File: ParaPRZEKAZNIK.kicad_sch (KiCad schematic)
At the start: 50 parts, among them J101 Screw_Terminal_01x03, J102 Screw_Terminal_01x03, J103 Screw_Terminal_01x03, J104 Screw_Terminal_01x03, J105 Screw_Terminal_01x03, J106 RJ45, U101 MAX31865xTP, U102 ST3232BTR, Y101 32k768

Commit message: schematic
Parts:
- added C1, C10, C15, C16, C2, C4, C6, C8, C9: 100n, Capacitor_SMD:C_0805_2012Metric_Pad1.18x1.45mm_HandSolder, symbol Device:C_Small
- added C13, C17: 1uF, Capacitor_SMD:C_0805_2012Metric_Pad1.18x1.45mm_HandSolder, symbol Device:C_Small
- added C14: 22uF, Capacitor_THT:CP_Radial_D8.0mm_P5.00mm, symbol Device:C_Polarized
- added C18: 100uF, Capacitor_THT:CP_Radial_D8.0mm_P5.00mm, symbol Device:C_Polarized
- added D1: 1N4001, Diode_THT:D_DO-41_SOD81_P10.16mm_Horizontal, symbol Diode:1N4001
- added D2: 1.0SMBJ5.0A, Diode_SMD:D_SMB, symbol Diode:SM6T6V8A
- added J1: PT1000, Connector_Phoenix_MC:PhoenixContact_MCV_1,5_4-G-3.81_1x04_P3.81mm_Vertical, symbol Connector:Screw_Terminal_01x04
- added J3: UC_CONTROL, Connector_Phoenix_MC:PhoenixContact_MCV_1,5_2-G-3.5_1x02_P3.50mm_Vertical, symbol Connector:Screw_Terminal_01x02
- added J4: MAIN_CONTROL, Connector_Phoenix_MC:PhoenixContact_MCV_1,5_3-G-3.5_1x03_P3.50mm_Vertical, symbol Connector:Screw_Terminal_01x03
- added J5: PROG, Connector_PinHeader_2.54mm:PinHeader_1x06_P2.54mm_Vertical, symbol Connector_Generic:Conn_01x06
- added L1, L2, L3, L4, L5: 4u7, Inductor_SMD:L_0805_2012Metric_Pad1.15x1.40mm_HandSolder, symbol Device:L_Ferrite
- added R1: 630, Resistor_SMD:R_0805_2012Metric_Pad1.20x1.40mm_HandSolder, symbol Device:R
- added R10, R11, R3, R5, R6: 10k, Resistor_SMD:R_0805_2012Metric_Pad1.20x1.40mm_HandSolder, symbol Device:R
- added R12, R13: 10k, Resistor_SMD:R_0805_2012Metric_Pad1.20x1.40mm_HandSolder, symbol Device:R_Small
- added R2: 120, Resistor_SMD:R_0805_2012Metric_Pad1.20x1.40mm_HandSolder, symbol Device:R
- added U2: SP3485EN, Package_SO:SOIC-8_3.9x4.9mm_P1.27mm, symbol Interface_UART:SP3485EN
- added U5: LM1117DT-3.3, Package_TO_SOT_SMD:TO-252-3_TabPin2, symbol Regulator_Linear:LM1117DT-3.3
- C11: renamed from C?; footprint (none) -> Capacitor_SMD:C_0805_2012Metric_Pad1.18x1.45mm_HandSolder
- C12: renamed from C103; value C -> 100n; footprint (none) -> Capacitor_SMD:C_0805_2012Metric_Pad1.18x1.45mm_HandSolder
- C19: renamed from C101; footprint (none) -> Capacitor_SMD:C_0805_2012Metric_Pad1.18x1.45mm_HandSolder
- C20: renamed from C102; footprint (none) -> Capacitor_SMD:C_0805_2012Metric_Pad1.18x1.45mm_HandSolder
- C3: renamed from C106; value C -> 100n; footprint (none) -> Capacitor_SMD:C_0805_2012Metric_Pad1.18x1.45mm_HandSolder
- C5: renamed from C105; value C -> 100n; footprint (none) -> Capacitor_SMD:C_0805_2012Metric_Pad1.18x1.45mm_HandSolder
- C7: renamed from C104; value C -> 100n; footprint (none) -> Capacitor_SMD:C_0805_2012Metric_Pad1.18x1.45mm_HandSolder
- D10, D11, D12, D13, D14: renamed from D?; value D_Schottky -> 1N5819HW-7-F; footprint (none) -> Diode_SMD:D_SOD-123
- J10: renamed from J105; footprint (none) -> Connector_Phoenix_MSTB:PhoenixContact_MSTBVA_2,5_3-G_1x03_P5.00mm_Vertical
- J2: renamed from J106; value RJ45 -> 5556416-1 TE Connectivity; footprint (none) -> Connector_RJ:RJ45_OST_PJ012-8P8CX_Vertical
- J6: renamed from J101; footprint (none) -> Connector_Phoenix_MSTB:PhoenixContact_MSTBVA_2,5_3-G_1x03_P5.00mm_Vertical
- J7: renamed from J102; footprint (none) -> Connector_Phoenix_MSTB:PhoenixContact_MSTBVA_2,5_3-G_1x03_P5.00mm_Vertical
- J8: renamed from J103; footprint (none) -> Connector_Phoenix_MSTB:PhoenixContact_MSTBVA_2,5_3-G_1x03_P5.00mm_Vertical
- J9: renamed from J104; footprint (none) -> Connector_Phoenix_MSTB:PhoenixContact_MSTBVA_2,5_3-G_1x03_P5.00mm_Vertical
- R4, R7, R8, R9: renamed from R?; footprint (none) -> Resistor_SMD:R_0805_2012Metric_Pad1.20x1.40mm_HandSolder
- RN1, RN2: renamed from RN?; footprint (none) -> Resistor_SMD:R_Array_Convex_4x1206; symbol Device:R_Pack05 -> Device:R_Pack04
- SW1: renamed from SW?; footprint (none) -> switches:Alps_SSSS222700
- U3: renamed from U102; footprint (none) -> Package_SO:TSSOP-16_4.4x5mm_P0.65mm
- U6: renamed from U?; footprint (none) -> Package_SO:TSOP-6_1.65x3.05mm_P0.95mm
- Y1: renamed from Y101; footprint (none) -> Crystal:Crystal_SMD_SeikoEpson_MC306-4Pin_8.0x3.2mm
- gave numbers to parts that had none: 19
- renumbered U101 to U1
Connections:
- net +5V is gone; now on net +3V3: R9.2
- net VCC is gone; now on net +3V3: U6.5 (VCC), U6.5 (VCC)
- net GND: now also J2.4, J2.5, U1.10 (GND), U1.15 (DGND), U1.16 (GND), U1.21 (GND), U3.15 (GND), C1.1, C10.1, C13.1, C14.2, C15.1, C16.1, C17.1, C18.2, C2.1, C4.1, C6.1, C8.1, C9.1, D2.2 (A2), J3.2 (Pin_2), J4.3 (Pin_3), J5.6 (Pin_6), R10.2, R11.2, R3.1, R6.1, U2.5 (GND), U5.1 (GND)
- net RESET: now also J5.5 (Pin_5), R11.1
- net SWCLK: now also J5.4 (Pin_4)
- net SWDIO: now also J5.3 (Pin_3)
- net +12V: now reaches D12.1 (K)
- net +12V: now also D10.1 (K), D11.1 (K), D13.1 (K), D14.1 (K), K1.2, K2.2, K3.2, K4.2, K5.2, C13.2, D1.1 (K), L5.1
- net at D12.2 (A): now also K3.9, Q4.3 (C)
- net CONTROL_SIG: now reaches R4.1
- net CONTROL_SIG: now also J4.2 (Pin_2)
- net USART2_TX: now reaches U3.11 (T1IN)
- net USART2_TX: now also U4.8 (PA2)
- net RS232_RX: now reaches U3.13 (R1IN)
- net RS232_RX: now also J2.6
- net RS232_TX: now reaches U3.14 (T1OUT)
- net RS232_TX: now also J2.3
- net +3V3: now reaches U3.16 (VCC)
- net +3V3: now also U1.19 (DVDD), U1.20 (VDD), U4.1 (VDD), U4.17 (VDD), U4.5 (VDDA), C10.2, C15.2, C16.2, C17.2, C18.1, C9.2, J5.1 (Pin_1), R5.2, U2.8 (VCC), U5.2 (VO)
- net USART2_RX: now reaches U3.9 (R2OUT)
- net USART2_RX: now also U4.9 (PA3)
- net at K5.9, Q6.3 (C): now also D14.2 (A)
- net F+: now reaches U1.5 (FORCE+)
- net F+: now also C1.2, L1.2
- net R+: now reaches U1.7 (RTDIN+)
- net R+: now also C2.2, L3.2
- net R-: now reaches U1.8 (RTDIN-)
- net R-: now also C4.2, L2.2
- net F-: now reaches U1.9 (FORCE-)
- net F-: now also C6.2, L4.2
- net BASE_R4: now reaches RN2.1 (R1.1)
- net BASE_R4: now also Q5.1 (B); no longer Q6.1 (B)
- net RELAYS_CTRL: now reaches D5.2 (A), D6.2 (A), D7.2 (A), D8.2 (A), D9.2 (A), U6.6
- net ACTIVE_HI: now reaches SW1.3 (C), U6.4
- net ACTIVE_LO: now reaches Q1.2 (E), R8.1, R9.1, SW1.1 (A), SW1.4 (A)
- net at K1.9, Q2.3 (C): now also D10.2 (A)
- net at D13.2 (A): now also K4.9, Q5.3 (C)
- net BASE_R1: now reaches RN2.4 (R4.1)
- net BASE_R1: now also Q2.1 (B); no longer Q3.1 (B)
- net at K2.9, Q3.3 (C): now also D11.2 (A)
- net BASE_R3: now reaches RN2.2 (R2.1)
- net BASE_R3: now also Q4.1 (B); no longer Q5.1 (B)
- net UC_R5: now reaches U4.30 (PB7)
- net UC_R5: now also R12.1; no longer RN1.10 (R1.2)
- net UC_R1: now reaches U4.26 (PB3)
- net UC_R1: now also RN1.5 (R4.2); no longer RN1.6 (R5.2)
- net UC_R2: now reaches U4.27 (PB4)
- net UC_R2: now also RN1.6 (R3.2); no longer RN1.7 (R4.2)
- net UC_R3: now reaches U4.28 (PB5)
- net UC_R3: now also RN1.7 (R2.2); no longer RN1.8 (R3.2)
- net UC_R4: now reaches U4.29 (PB6)
- net UC_R4: now also RN1.8 (R1.2); no longer RN1.9 (R2.2)
- net R1: now reaches RN2.5 (R4.2)
- net R1: now also D5.1 (K), RN1.4 (R4.1); no longer Q2.1 (B)
- net MICRO_CTRL: now reaches U4.15 (PB1)
- net MICRO_CTRL: now also C8.2, D2.1 (A1), R1.2, R3.2
- net USART1_TX: now reaches U4.19 (PA9)
- net USART1_TX: now also R6.2, U2.4 (DI)
- net USART1_RX: now reaches U4.20 (PA10)
- net USART1_RX: now also U2.1 (RO)
- net USART1_DE: now reaches U4.22 (PA12)
- net USART1_DE: now also R5.1, U2.2 (~{RE}), U2.3 (DE)
- net BOOT0: now reaches U4.31 (BOOT0)
- net BOOT0: now also J5.2 (Pin_2), R10.1
- net BASE_R2: now reaches RN2.3 (R3.1)
- net BASE_R2: now also Q3.1 (B); no longer Q4.1 (B)
- new net: J3.1 (Pin_1), R1.1
- new net: J1.3 (Pin_3), L2.1
- new net: R2.2, U2.6 (A)
- new net: R2.1, U2.7 (B)
- new net: C14.1, L5.2, U5.3 (VI)
- new net: D1.2 (A), J4.1 (Pin_1)
- new net: J1.1 (Pin_1), L1.1
- new net: J1.2 (Pin_2), L3.1
- new net: J1.4 (Pin_4), L4.1
- new net BASE_R5: Q6.1 (B), R13.2
- new net R2: D6.1 (K), RN1.3 (R3.1), RN2.6 (R3.2)
- new net R3: D7.1 (K), RN1.2 (R2.1), RN2.7 (R2.2)
- new net R4: D8.1 (K), RN1.1 (R1.1), RN2.8 (R1.2)
- new net R5: D9.1 (K), R12.2, R13.1
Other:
- note removed: "ACTIVE HI"
- moved on the sheet: C12, C3, C5, C7, D4, J2, R7, U1, U3, U6B

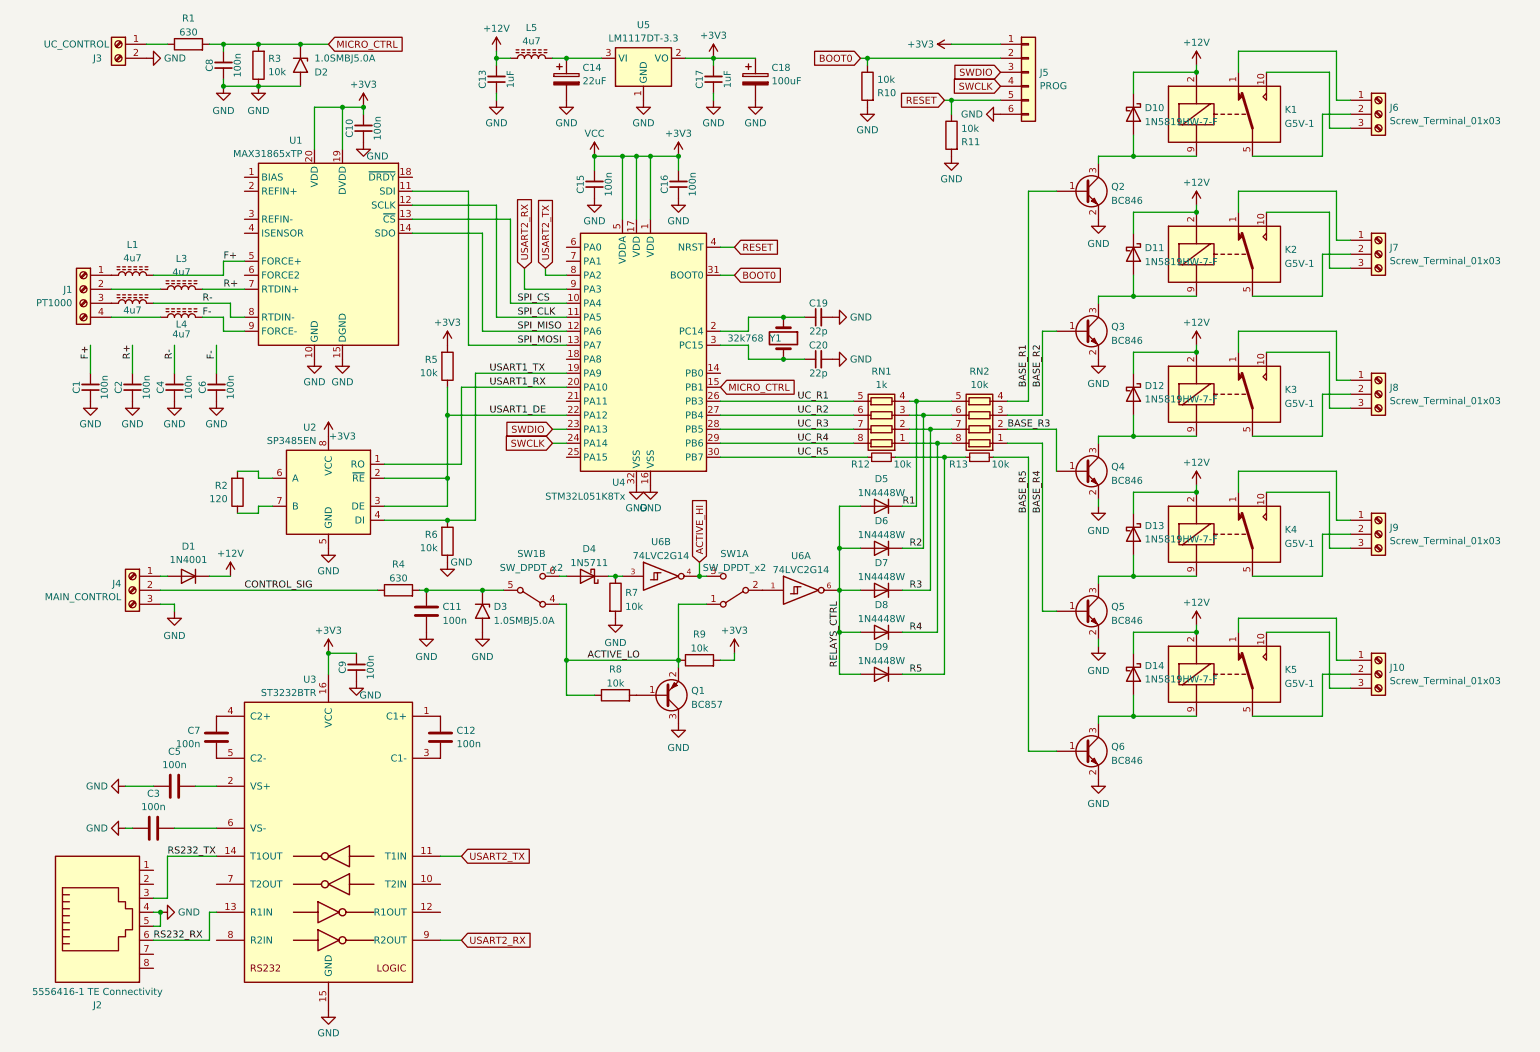
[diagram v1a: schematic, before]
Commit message: componets placed on pcb
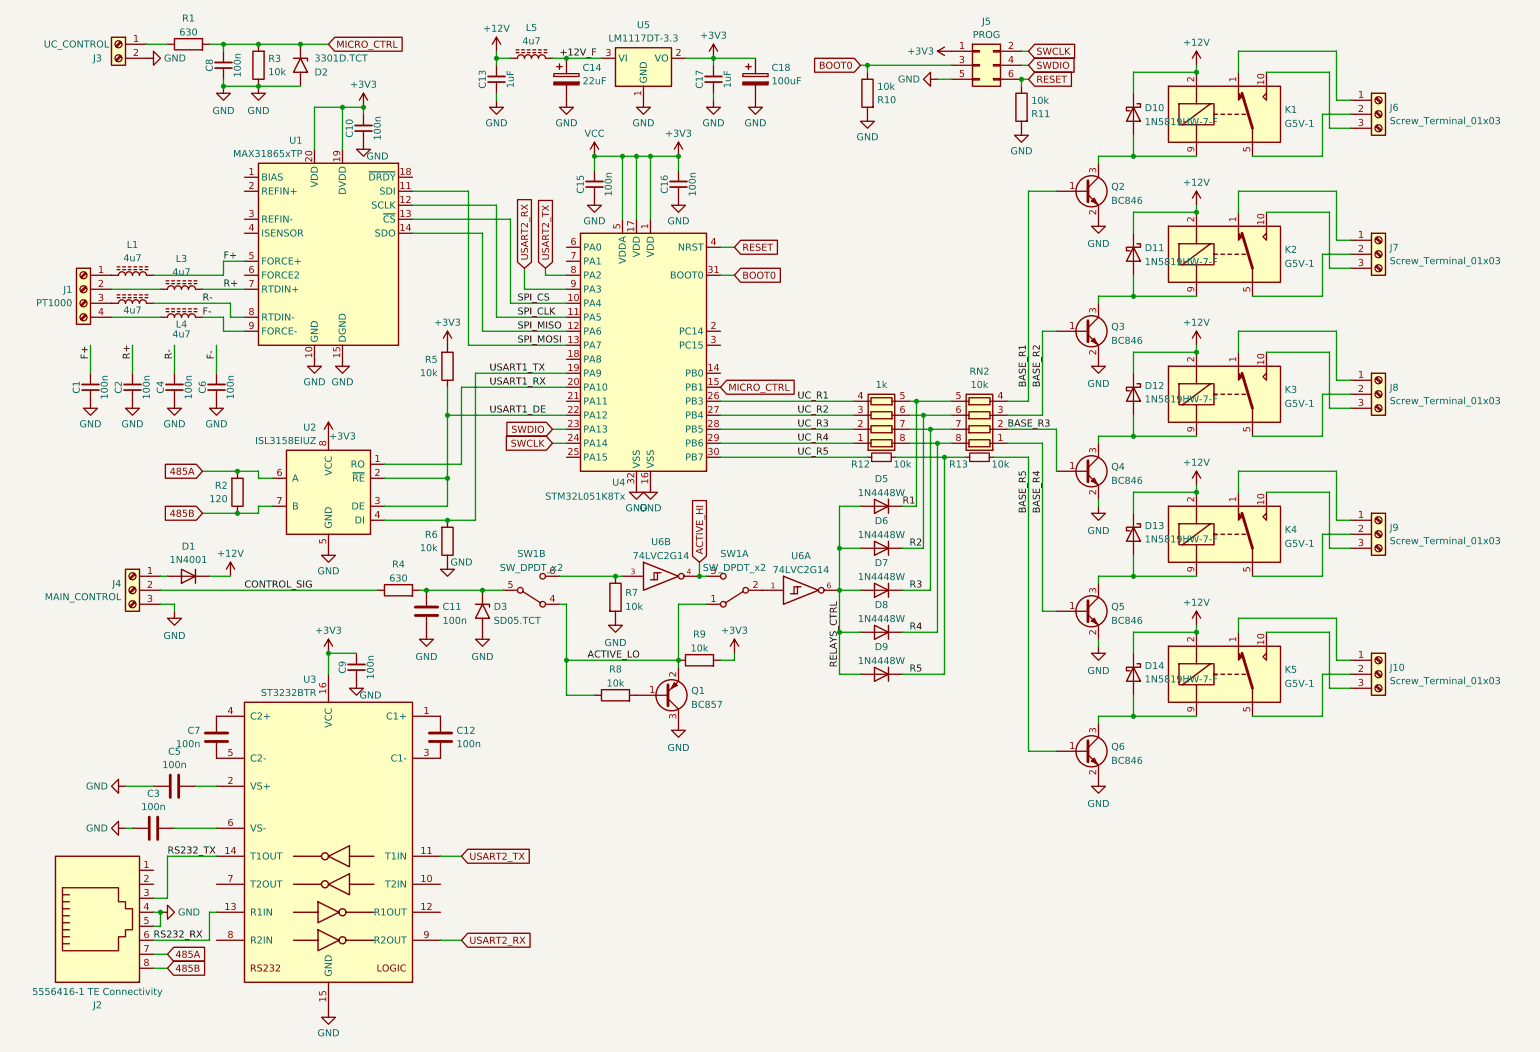
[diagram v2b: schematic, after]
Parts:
- removed C19, C20: 22p, Capacitor_SMD:C_0805_2012Metric_Pad1.18x1.45mm_HandSolder, symbol Device:C_Small
- removed D4: 1N5711, Diode_THT:D_DO-35_SOD27_P7.62mm_Horizontal, symbol Diode:1N5711
- removed Y1: 32k768, Crystal:Crystal_SMD_SeikoEpson_MC306-4Pin_8.0x3.2mm, symbol Device:Crystal
- C18: footprint Capacitor_THT:CP_Radial_D8.0mm_P5.00mm -> Capacitor_Tantalum_SMD:CP_EIA-3528-21_Kemet-B_Pad1.50x2.35mm_HandSolder
- D1: footprint Diode_THT:D_DO-41_SOD81_P10.16mm_Horizontal -> Diode_SMD:D_SMB
- D2: value 1.0SMBJ5.0A -> 3301D.TCT; footprint Diode_SMD:D_SMB -> Diode_SMD:D_SOD-323_HandSoldering
- D3: value 1.0SMBJ5.0A -> SD05.TCT; footprint Diode_SMD:D_SMB -> Diode_SMD:D_SOD-323_HandSoldering
- J10, J6, J7, J8, J9: footprint Connector_Phoenix_MSTB:PhoenixContact_MSTBVA_2,5_3-G_1x03_P5.00mm_Vertical -> Connector_Phoenix_MC:PhoenixContact_MCV_1,5_3-G-3.5_1x03_P3.50mm_Vertical
- J5: footprint Connector_PinHeader_2.54mm:PinHeader_1x06_P2.54mm_Vertical -> Connector_PinHeader_2.54mm:PinHeader_2x03_P2.54mm_Vertical; symbol Connector_Generic:Conn_01x06 -> Connector_Generic:Conn_02x03_Odd_Even
- U2: value SP3485EN -> ISL3158EIUZ; footprint Package_SO:SOIC-8_3.9x4.9mm_P1.27mm -> Package_SO:MSOP-8_3x3mm_P0.65mm
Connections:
- net BOOT0: now also J5.3 (Pin_3); no longer J5.2 (Pin_2)
- net GND: now also J5.5 (Pin_5); no longer J5.6 (Pin_6)
- net R1: now also RN1.5 (R4.2); no longer RN1.4 (R4.1)
- net R2: now also RN1.6 (R3.2); no longer RN1.3 (R3.1)
- net R3: now also RN1.7 (R2.2); no longer RN1.2 (R2.1)
- net R4: now also RN1.8 (R1.2); no longer RN1.1 (R1.1)
- net RESET: now also J5.6 (Pin_6); no longer J5.5 (Pin_5)
- net SWCLK: now also J5.2 (Pin_2); no longer J5.4 (Pin_4)
- net SWDIO: now also J5.4 (Pin_4); no longer J5.3 (Pin_3)
- net UC_R1: now also RN1.4 (R4.1); no longer RN1.5 (R4.2)
- net UC_R2: now also RN1.3 (R3.1); no longer RN1.6 (R3.2)
- net UC_R3: now also RN1.2 (R2.1); no longer RN1.7 (R2.2)
- net UC_R4: now also RN1.1 (R1.1); no longer RN1.8 (R1.2)
- net 485A: now reaches R2.2, U2.6 (A)
- net 485A: now also J2.7
- net 485B: now reaches R2.1, U2.7 (B)
- net 485B: now also J2.8
- net +12V_F: now reaches C14.1, L5.2, U5.3 (VI)
- net at R7.1, U6.3: now also SW1.6 (C)
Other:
- moved on the sheet: J5, R10, R11

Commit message: partially routed
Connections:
- net +12V_F is gone; now on net +12V: C14.1, L5.2, U5.3 (VI)
- net +12V: no longer C13.2, D1.1 (K), L5.1
- net F+: no longer U1.5 (FORCE+)
- new net +BATT: C13.2, D1.1 (K), L5.1
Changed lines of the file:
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@@
+    (stroke (width 0) (type default))
+  )
+  (wire (pts (xy 109.22 19.05) (xy 109.22 20.32))
     (stroke (width 0) (type default))
   )
@@
     (stroke (width 0) (type default))
   )
-  (wire (pts (xy 46.99 57.15) (xy 50.8 57.15))
+  (wire (pts (xy 46.99 57.15) (xy 43.18 57.15))
     (stroke (width 0) (type default))
   )
@@
   )
   (label "BASE_R2" (at 195.58 80.01 90) (fields_autoplaced)
-    (effects (font (size 1.27 1.27)) (justify left bottom))
-  )
-  (label "+12V_F" (at 107.95 20.32 0) (fields_autoplaced)
     (effects (font (size 1.27 1.27)) (justify left bottom))
   )
@@
     )
   )
+  (symbol (lib_id "power:+BATT") (at 48.26 114.3 0) (unit 1)
+    (in_bom yes) (on_board yes) (dnp no) (fields_autoplaced)
+    (property "Reference" "#PWR042" (at 48.26 118.11 0)
+      (effects (font (size 1.27 1.27)) hide)
+    )
+    (property "Value" "+BATT" (at 48.26 110.1669 0)
+      (effects (font (size 1.27 1.27)))
+    )
+    (property "Footprint" "" (at 48.26 114.3 0)
+      (effects (font (size 1.27 1.27)) hide)
+    )
+    (property "Datasheet" "" (at 48.26 114.3 0)
+      (effects (font (size 1.27 1.27)) hide)
+    )
+    (pin "1")
+    (instances
+      (project "ParaPRZEKAZNIK"
+        (path "/e63e39d7-6ac0-4ffd-8aa3-1841a4541b55"
+          (reference "#PWR042") (unit 1)
+        )
+      )
+    )
+  )
   (symbol (lib_id "Device:C_Small") (at 46.99 21.59 180) (unit 1)
     (in_bom yes) (on_board yes) (dnp no)
@@
     )
   )
+  (symbol (lib_id "power:+BATT") (at 96.52 19.05 0) (unit 1)
+    (in_bom yes) (on_board yes) (dnp no) (fields_autoplaced)
+    (property "Reference" "#PWR011" (at 96.52 22.86 0)
+      (effects (font (size 1.27 1.27)) hide)
+    )
+    (property "Value" "+BATT" (at 96.52 14.9169 0)
+      (effects (font (size 1.27 1.27)))
+    )
+    (property "Footprint" "" (at 96.52 19.05 0)
+      (effects (font (size 1.27 1.27)) hide)
+    )
+    (property "Datasheet" "" (at 96.52 19.05 0)
+      (effects (font (size 1.27 1.27)) hide)
+    )
+    (pin "1")
+    (instances
+      (project "ParaPRZEKAZNIK"
+        (path "/e63e39d7-6ac0-4ffd-8aa3-1841a4541b55"
+          (reference "#PWR011") (unit 1)
+        )
+      )
+    )
+  )
   (symbol (lib_id "Device:D_Schottky") (at 212.09 106.68 270) (unit 1)
     (in_bom yes) (on_board yes) (dnp no) (fields_autoplaced)
@@
     )
   )
-  (symbol (lib_id "power:+12V") (at 96.52 19.05 0) (unit 1)
-    (in_bom yes) (on_board yes) (dnp no) (fields_autoplaced)
-    (property "Reference" "#PWR026" (at 96.52 22.86 0)
-      (effects (font (size 1.27 1.27)) hide)
-    )
-    (property "Value" "+12V" (at 96.52 14.9169 0)
-      (effects (font (size 1.27 1.27)))
-    )
-    (property "Footprint" "" (at 96.52 19.05 0)
-      (effects (font (size 1.27 1.27)) hide)
-    )
-    (property "Datasheet" "" (at 96.52 19.05 0)
+  (symbol (lib_id "power:+12V") (at 109.22 19.05 0) (unit 1)
+    (in_bom yes) (on_board yes) (dnp no) (fields_autoplaced)
+    (property "Reference" "#PWR026" (at 109.22 22.86 0)
+      (effects (font (size 1.27 1.27)) hide)
+    )
+    (property "Value" "+12V" (at 109.22 14.9169 0)
+      (effects (font (size 1.27 1.27)))
+    )
+    (property "Footprint" "" (at 109.22 19.05 0)
+      (effects (font (size 1.27 1.27)) hide)
+    )
+    (property "Datasheet" "" (at 109.22 19.05 0)
       (effects (font (size 1.27 1.27)) hide)
     )
@@
         )
       )
-    )
-  )
-  (symbol (lib_id "power:+12V") (at 48.26 114.3 0) (unit 1)
-    (in_bom yes) (on_board yes) (dnp no) (fields_autoplaced)
-    (property "Reference" "#PWR011" (at 48.26 118.11 0)
-      (effects (font (size 1.27 1.27)) hide)
-    )
-    (property "Value" "+12V" (at 48.26 110.1669 0)
-      (effects (font (size 1.27 1.27)))
-    )
-    (property "Footprint" "" (at 48.26 114.3 0)
-      (effects (font (size 1.27 1.27)) hide)
-    )
-    (property "Datasheet" "" (at 48.26 114.3 0)
-      (effects (font (size 1.27 1.27)) hide)
-    )
-    (pin "1")
-    (instances
-      (project "ParaPRZEKAZNIK"
-        (path "/e63e39d7-6ac0-4ffd-8aa3-1841a4541b55"
-          (reference "#PWR011") (unit 1)
-        )
-      )

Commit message: done and exported
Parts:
- added R14: R, Resistor_SMD:R_0805_2012Metric_Pad1.20x1.40mm_HandSolder, symbol Device:R
- added R15: 20k, Resistor_SMD:R_0805_2012Metric_Pad1.20x1.40mm_HandSolder, symbol Device:R
- added R16: 120, Resistor_SMD:R_0805_2012Metric_Pad1.20x1.40mm_HandSolder, symbol Device:R
- RN1: value 1k -> 10k
- RN2: value 10k -> 1k
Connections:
- net +3V3: now also R15.2
- net 485A: now also R15.1
- net 485B: now also R16.2
- net F+: now also U1.5 (FORCE+)
- net GND: now also U1.6 (FORCE2), R16.1
- net at U1.1 (BIAS): now also U1.2 (REFIN+), R14.1
- net at U1.3 (REFIN-): now also U1.4 (ISENSOR), R14.2
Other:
- company: (none) -> ML Elektronika Mateusz Lubecki
- title: (none) -> ParaPRZEKAZNIK
- moved on the sheet: C1, C2, C4, C6, D1, J4, R2
